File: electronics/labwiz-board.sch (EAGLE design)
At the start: 133 parts, among them IC1 MCP3424, J1 SD_MICRO_SDIO_1BIT, J2 CORTEX_DEBUGSMD, J30 4P-SMD-2.0-90D, J4 4P-SMD-2.0-90D, J5 4P-SMD-2.0-90D, U1 STM32F10XRXT6, U4 MIC5219-3.3V, X2 M12_BOTTOM_CONTACTS_FPC_1MM, Y1 32.768kHz, Y3 32.768kHz

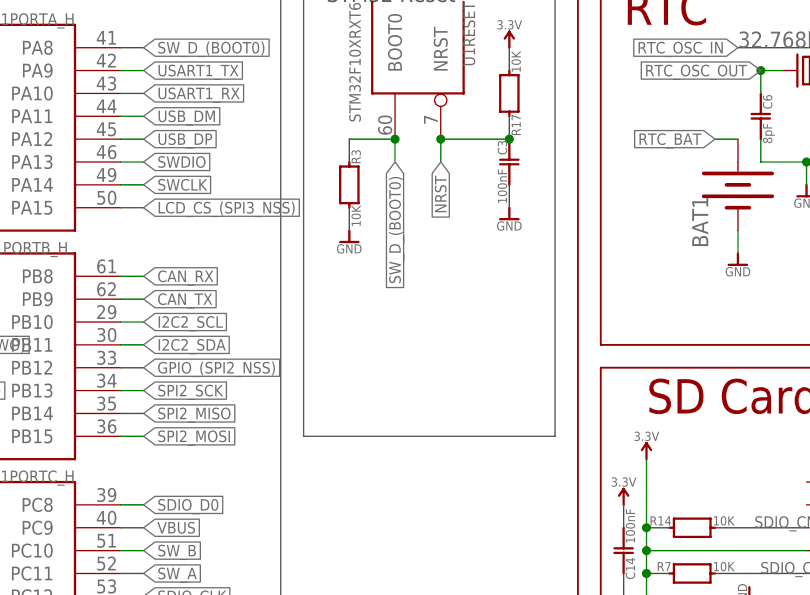
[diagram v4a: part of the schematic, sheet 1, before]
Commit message: Added solder jumper for BOOT0. Closes #22.
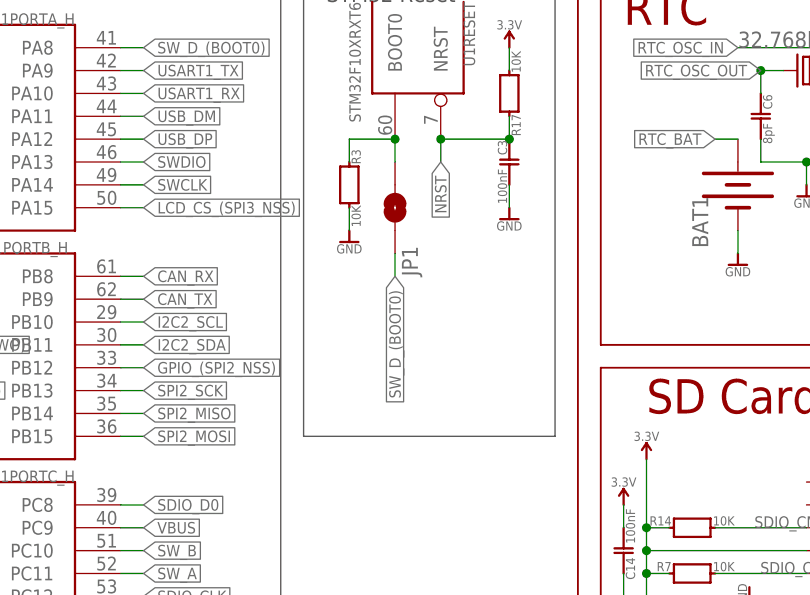
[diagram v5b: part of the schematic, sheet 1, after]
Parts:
- added JP1: JUMPER-PAD-2-NOYES_SILK, SparkFun-Passives:JUMPER-PAD-2-NOYES_SILK
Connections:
- new net N$69: JP1.2, R3.2, U1RESET.BOOT0
- net SW_D_(BOOT0): now also JP1.1; no longer R3.2, U1RESET.BOOT0
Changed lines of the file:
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@@
 <part name="R17" library="PaxInstruments-RCL" deviceset="R0402" device="_10K" value="10K"/>
 <part name="SUPPLY23" library="PaxInstruments-Aesthetics" deviceset="SYM_VCC" device="" technology="3.3V" value="3.3V"/>
+<part name="JP1" library="SparkFun-Passives" deviceset="JUMPER-PAD-2-NO" device="YES_SILK"/>
 </parts>
 <sheets>
@@
 <instance part="R17" gate="G$1" x="104.14" y="76.2" rot="MR0"/>
 <instance part="SUPPLY23" gate="G$1" x="104.14" y="81.28"/>
+<instance part="JP1" gate="G$1" x="91.44" y="63.5" smashed="yes" rot="R90">
+<attribute name="NAME" x="93.98" y="55.88" size="1.778" layer="95" rot="R90"/>
+</instance>
 </instances>
 <busses>
@@
 </segment>
 <segment>
-<pinref part="U1" gate="RESET" pin="BOOT0"/>
-<wire x1="91.44" y1="71.12" x2="91.44" y2="68.58" width="0.1524" layer="91"/>
-<label x="91.44" y="68.58" size="1.27" layer="95" rot="R270" xref="yes"/>
-<pinref part="R3" gate="G$1" pin="2"/>
-<wire x1="86.36" y1="68.58" x2="86.36" y2="71.12" width="0.1524" layer="91"/>
-<wire x1="86.36" y1="71.12" x2="91.44" y2="71.12" width="0.1524" layer="91"/>
-<junction x="91.44" y="71.12"/>
+<label x="91.44" y="55.88" size="1.27" layer="95" rot="R270" xref="yes"/>
+<pinref part="JP1" gate="G$1" pin="1"/>
+<wire x1="91.44" y1="58.42" x2="91.44" y2="55.88" width="0.1524" layer="91"/>
 </segment>
 </net>
@@
 </segment>
 </net>
+<net name="N$69" class="0">
+<segment>
+<pinref part="U1" gate="RESET" pin="BOOT0"/>
+<wire x1="86.36" y1="71.12" x2="91.44" y2="71.12" width="0.1524" layer="91"/>
+<pinref part="R3" gate="G$1" pin="2"/>
+<wire x1="86.36" y1="68.58" x2="86.36" y2="71.12" width="0.1524" layer="91"/>
+<wire x1="91.44" y1="71.12" x2="91.44" y2="68.58" width="0.1524" layer="91"/>
+<junction x="91.44" y="71.12"/>
+<pinref part="JP1" gate="G$1" pin="2"/>
+</segment>
+</net>

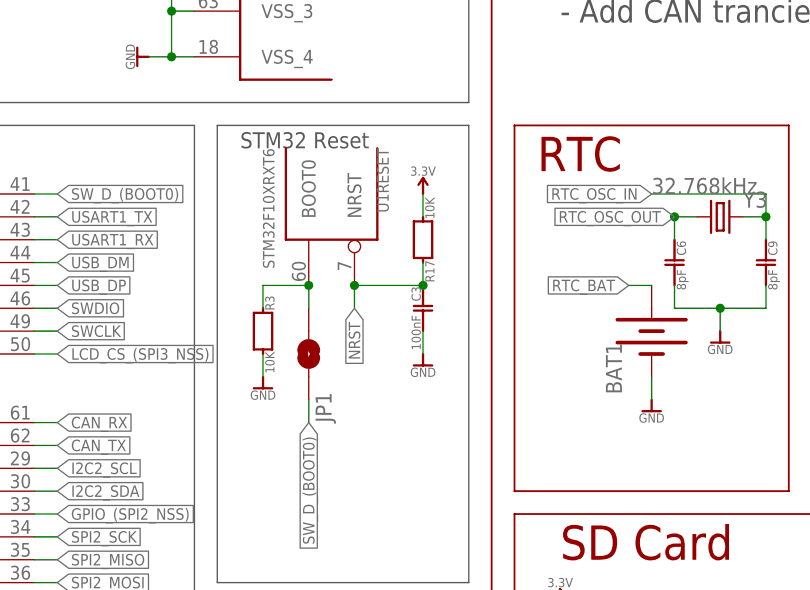
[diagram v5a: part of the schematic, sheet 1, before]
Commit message: Added RESET switch.
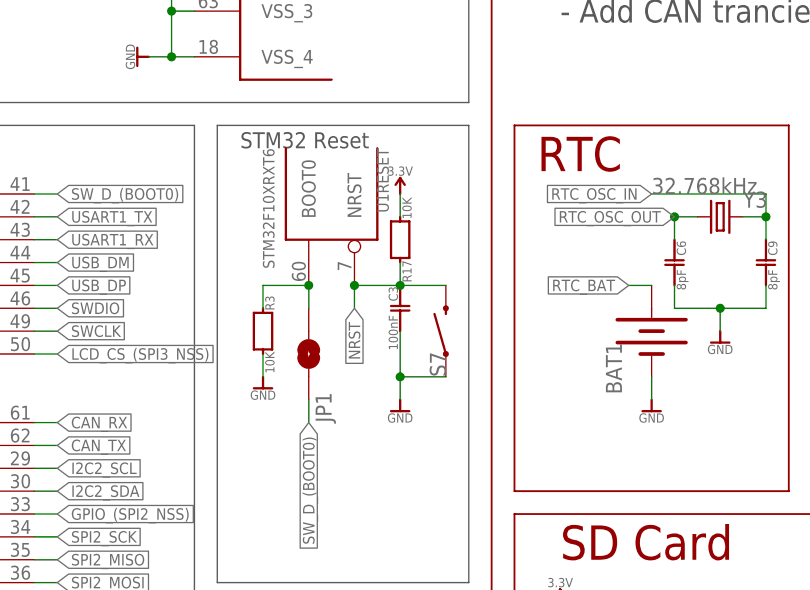
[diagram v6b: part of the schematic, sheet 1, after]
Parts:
- added S7: SWITCH-MOMENTARY-2SMD-3, PaxInstruments-Electromechanical:SWITCH-MOMENTARY-2SMD-3
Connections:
- net GND: now also S7.1
- net NRST: now also S7.2
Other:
- moved on the sheet: C3, R17
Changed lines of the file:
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@@
 <part name="SUPPLY23" library="PaxInstruments-Aesthetics" deviceset="SYM_VCC" device="" technology="3.3V" value="3.3V"/>
 <part name="JP1" library="SparkFun-Passives" deviceset="JUMPER-PAD-2-NO" device="YES_SILK"/>
+<part name="S7" library="PaxInstruments-Electromechanical" deviceset="SWITCH-MOMENTARY-2" device="SMD-3"/>
 </parts>
 <sheets>
@@
 <instance part="GND2" gate="G$1" x="73.66" y="96.52" rot="R270"/>
 <instance part="GND8" gate="G$1" x="27.94" y="134.62" rot="R90"/>
-<instance part="GND10" gate="G$1" x="104.14" y="63.5" rot="MR0"/>
-<instance part="C3" gate="G$1" x="104.14" y="68.58" rot="MR180"/>
+<instance part="GND10" gate="G$1" x="101.6" y="58.42" rot="MR0"/>
+<instance part="C3" gate="G$1" x="101.6" y="68.58" rot="MR180"/>
 <instance part="C10" gate="G$1" x="261.62" y="71.12" rot="MR90"/>
 <instance part="C11" gate="G$1" x="73.66" y="137.16" rot="MR270"/>
@@
 </instance>
 <instance part="P+4" gate="G$1" x="259.08" y="119.38" rot="MR0"/>
-<instance part="R17" gate="G$1" x="104.14" y="76.2" rot="MR0"/>
-<instance part="SUPPLY23" gate="G$1" x="104.14" y="81.28"/>
+<instance part="R17" gate="G$1" x="101.6" y="76.2" rot="MR0"/>
+<instance part="SUPPLY23" gate="G$1" x="101.6" y="81.28"/>
 <instance part="JP1" gate="G$1" x="91.44" y="63.5" smashed="yes" rot="R90">
 <attribute name="NAME" x="93.98" y="55.88" size="1.778" layer="95" rot="R90"/>
+</instance>
+<instance part="S7" gate="G$1" x="106.68" y="66.04" smashed="yes" rot="R90">
+<attribute name="NAME" x="106.68" y="60.96" size="1.778" layer="95" rot="R90"/>
 </instance>
 </instances>
@@
 <pinref part="R17" gate="G$1" pin="1"/>
 <pinref part="SUPPLY23" gate="G$1" pin="3.3V"/>
-<wire x1="104.14" y1="78.74" x2="104.14" y2="81.28" width="0.1524" layer="91"/>
+<wire x1="101.6" y1="78.74" x2="101.6" y2="81.28" width="0.1524" layer="91"/>
 </segment>
 </net>
@@
 <pinref part="GND10" gate="G$1" pin="GND"/>
 <pinref part="C3" gate="G$1" pin="2"/>
-<wire x1="104.14" y1="63.5" x2="104.14" y2="66.04" width="0.1524" layer="91"/>
+<wire x1="101.6" y1="58.42" x2="101.6" y2="60.96" width="0.1524" layer="91"/>
+<pinref part="S7" gate="G$1" pin="1"/>
+<wire x1="101.6" y1="60.96" x2="101.6" y2="66.04" width="0.1524" layer="91"/>
+<wire x1="106.68" y1="60.96" x2="101.6" y2="60.96" width="0.1524" layer="91"/>
+<junction x="101.6" y="60.96"/>
 </segment>
 <segment>
@@
 <wire x1="96.52" y1="71.12" x2="96.52" y2="68.58" width="0.1524" layer="91"/>
 <label x="96.52" y="68.58" size="1.27" layer="95" rot="R270" xref="yes"/>
-<wire x1="104.14" y1="71.12" x2="96.52" y2="71.12" width="0.1524" layer="91"/>
+<wire x1="101.6" y1="71.12" x2="96.52" y2="71.12" width="0.1524" layer="91"/>
 <junction x="96.52" y="71.12"/>
 <pinref part="R17" gate="G$1" pin="2"/>
-<wire x1="104.14" y1="71.12" x2="104.14" y2="73.66" width="0.1524" layer="91"/>
-<junction x="104.14" y="71.12"/>
-</segment>
-<segment>
+<wire x1="101.6" y1="71.12" x2="101.6" y2="73.66" width="0.1524" layer="91"/>
+<junction x="101.6" y="71.12"/>
+<pinref part="S7" gate="G$1" pin="2"/>
+<wire x1="106.68" y1="71.12" x2="101.6" y2="71.12" width="0.1524" layer="91"/>
+</segment>
+<segment>

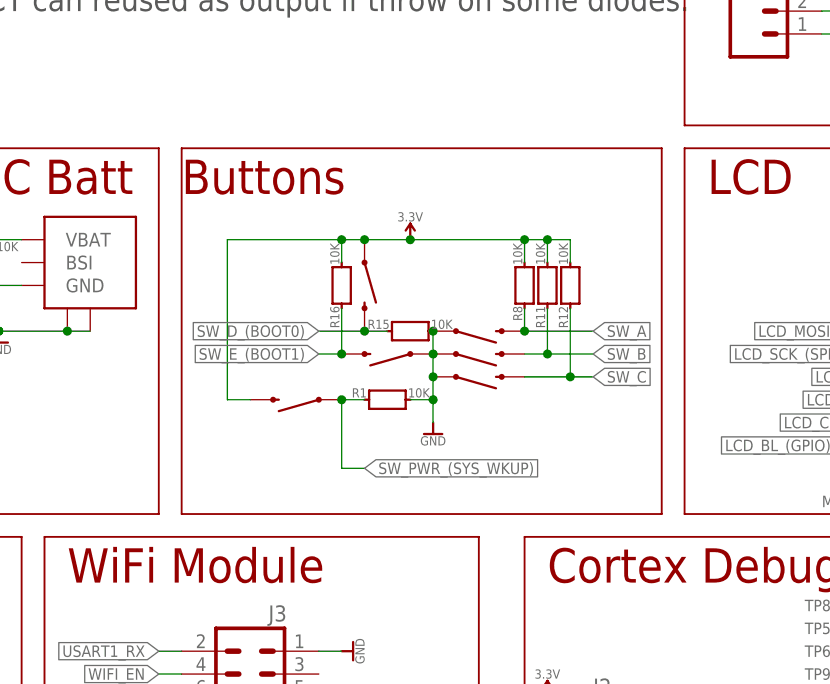
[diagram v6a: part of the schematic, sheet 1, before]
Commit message: Added BOOT0 jumper label. Added 100 nF caps to debounce switches.
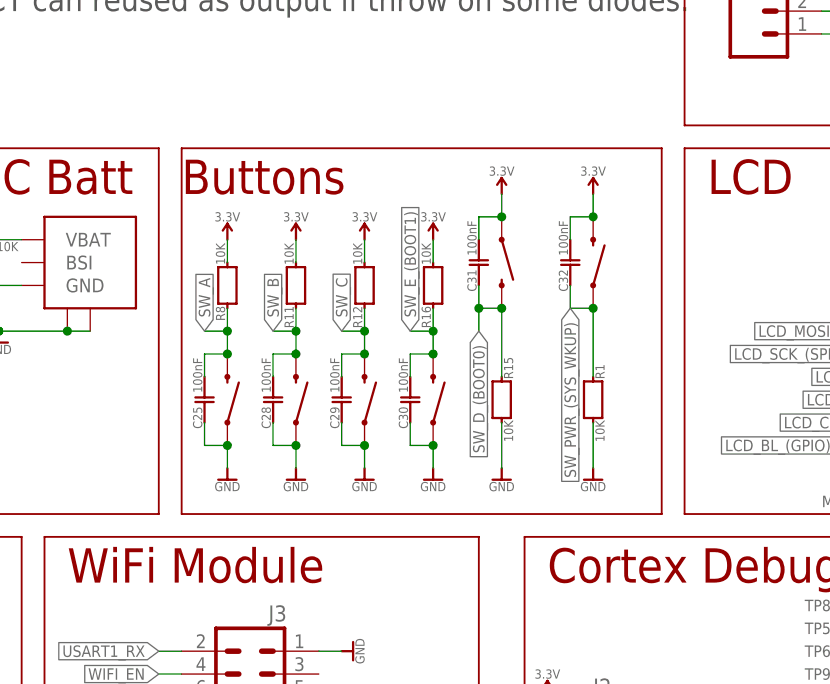
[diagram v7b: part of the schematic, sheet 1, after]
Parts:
- added C25, C28, C29, C30, C31, C32: 100nF, PaxInstruments-RCL:C0402_100NF
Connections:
- net 3.3V: now also C31.2, C32.2
- net GND: now also C25.1, C28.1, C29.1, C30.1
- net SW_A: now also C25.2
- net SW_B: now also C28.2
- net SW_C: now also C29.2
- net SW_D_(BOOT0): now also C31.1
- net SW_E_(BOOT1): now also C30.2
- net SW_PWR_(SYS_WKUP): now also C32.1
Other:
- moved on the sheet: R1, R11, R12, R15, R16, R8

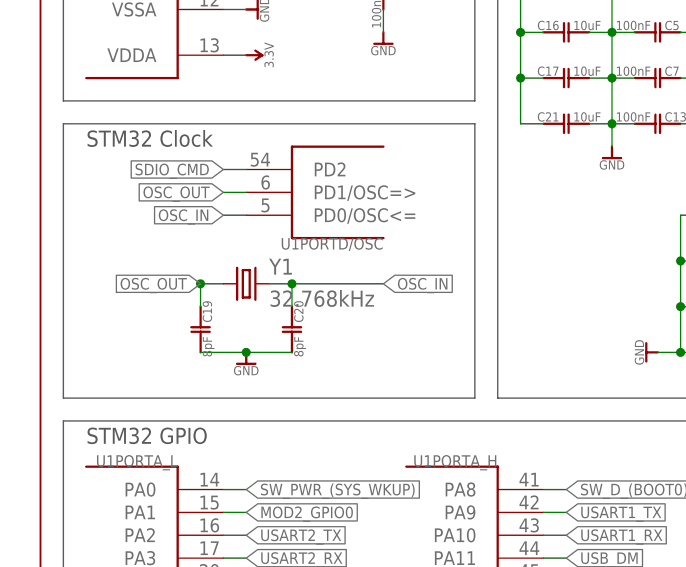
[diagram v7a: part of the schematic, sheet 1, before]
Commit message: Swapped 8 MHz crystal for a commong footprint in HQB.
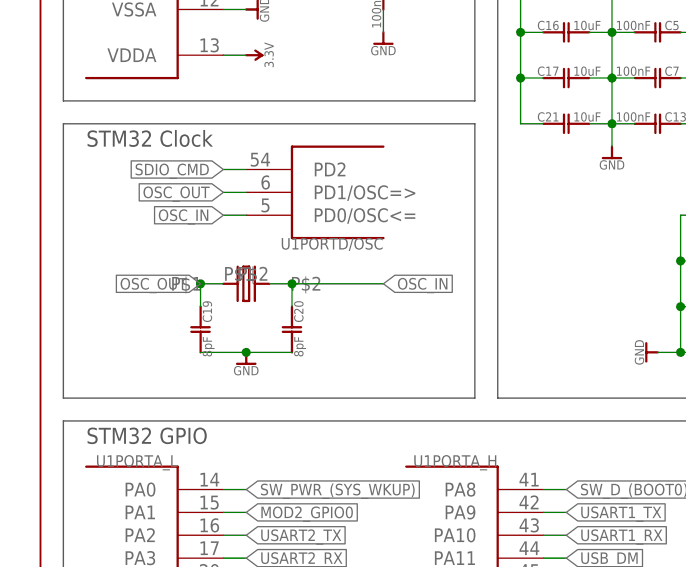
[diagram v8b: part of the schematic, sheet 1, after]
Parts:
- removed Y1: 32.768kHz, SparkFun-FreqCtrl:CRYSTAL3.2X1.5MM
- added U$9: NX3225GD, PaxInstruments-FreqCtrl:NX3225GD
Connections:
- net OSC_IN: now also U$9.P$2; no longer Y1.2
- net OSC_OUT: now also U$9.P$1; no longer Y1.1
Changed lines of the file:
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@@
 <part name="C19" library="PaxInstruments-RCL" deviceset="C0402" device="_8PF" value="8pF"/>
 <part name="C20" library="PaxInstruments-RCL" deviceset="C0402" device="_8PF" value="8pF"/>
-<part name="Y1" library="SparkFun-FreqCtrl" deviceset="CRYSTAL" device="3.2X1.5MM" value="32.768kHz"/>
 <part name="C21" library="PaxInstruments-RCL" deviceset="C0402" device="_10UF" value="10uF"/>
 <part name="MODULE1" library="PaxInstruments-Connectors" deviceset="PAX_MODULE" device="_EDGE_FEMALE_HOST" value="PI-module-female"/>
@@
 <part name="C31" library="PaxInstruments-RCL" deviceset="C0402" device="_100NF" value="100nF"/>
 <part name="C32" library="PaxInstruments-RCL" deviceset="C0402" device="_100NF" value="100nF"/>
+<part name="U$9" library="PaxInstruments-FreqCtrl" deviceset="NX3225GD" device=""/>
 </parts>
 <sheets>
@@
 <instance part="C19" gate="G$1" x="22.86" y="99.06" rot="R180"/>
 <instance part="C20" gate="G$1" x="33.02" y="99.06" rot="R180"/>
-<instance part="Y1" gate="G$1" x="27.94" y="104.14"/>
 <instance part="C21" gate="G$1" x="63.5" y="121.92" rot="R270"/>
 <instance part="MODULE1" gate="G$1" x="40.64" y="223.52"/>
@@
 <instance part="C31" gate="G$1" x="213.36" y="76.2"/>
 <instance part="C32" gate="G$1" x="223.52" y="76.2"/>
+<instance part="U$9" gate="G$1" x="27.94" y="104.14"/>
 </instances>
 <busses>
@@
 <wire x1="33.02" y1="104.14" x2="33.02" y2="101.6" width="0.1524" layer="91"/>
 <wire x1="30.48" y1="104.14" x2="33.02" y2="104.14" width="0.1524" layer="91"/>
-<pinref part="Y1" gate="G$1" pin="2"/>
 <wire x1="43.18" y1="104.14" x2="33.02" y2="104.14" width="0.1524" layer="91"/>
 <junction x="33.02" y="104.14"/>
+<pinref part="U$9" gate="G$1" pin="P$2"/>
 </segment>
 </net>
@@
 <wire x1="22.86" y1="104.14" x2="22.86" y2="101.6" width="0.1524" layer="91"/>
 <junction x="22.86" y="104.14"/>
-<pinref part="Y1" gate="G$1" pin="1"/>
 <label x="22.86" y="104.14" size="1.27" layer="95" rot="R180" xref="yes"/>
-</segment>
-</net>
+<pinref part="U$9" gate="G$1" pin="P$1"/>
+</segment>
+</net>
